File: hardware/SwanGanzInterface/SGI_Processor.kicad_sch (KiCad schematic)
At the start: 10 parts, among them U7 LP-MSPM0G3507, U8 Adafruit ST7735R

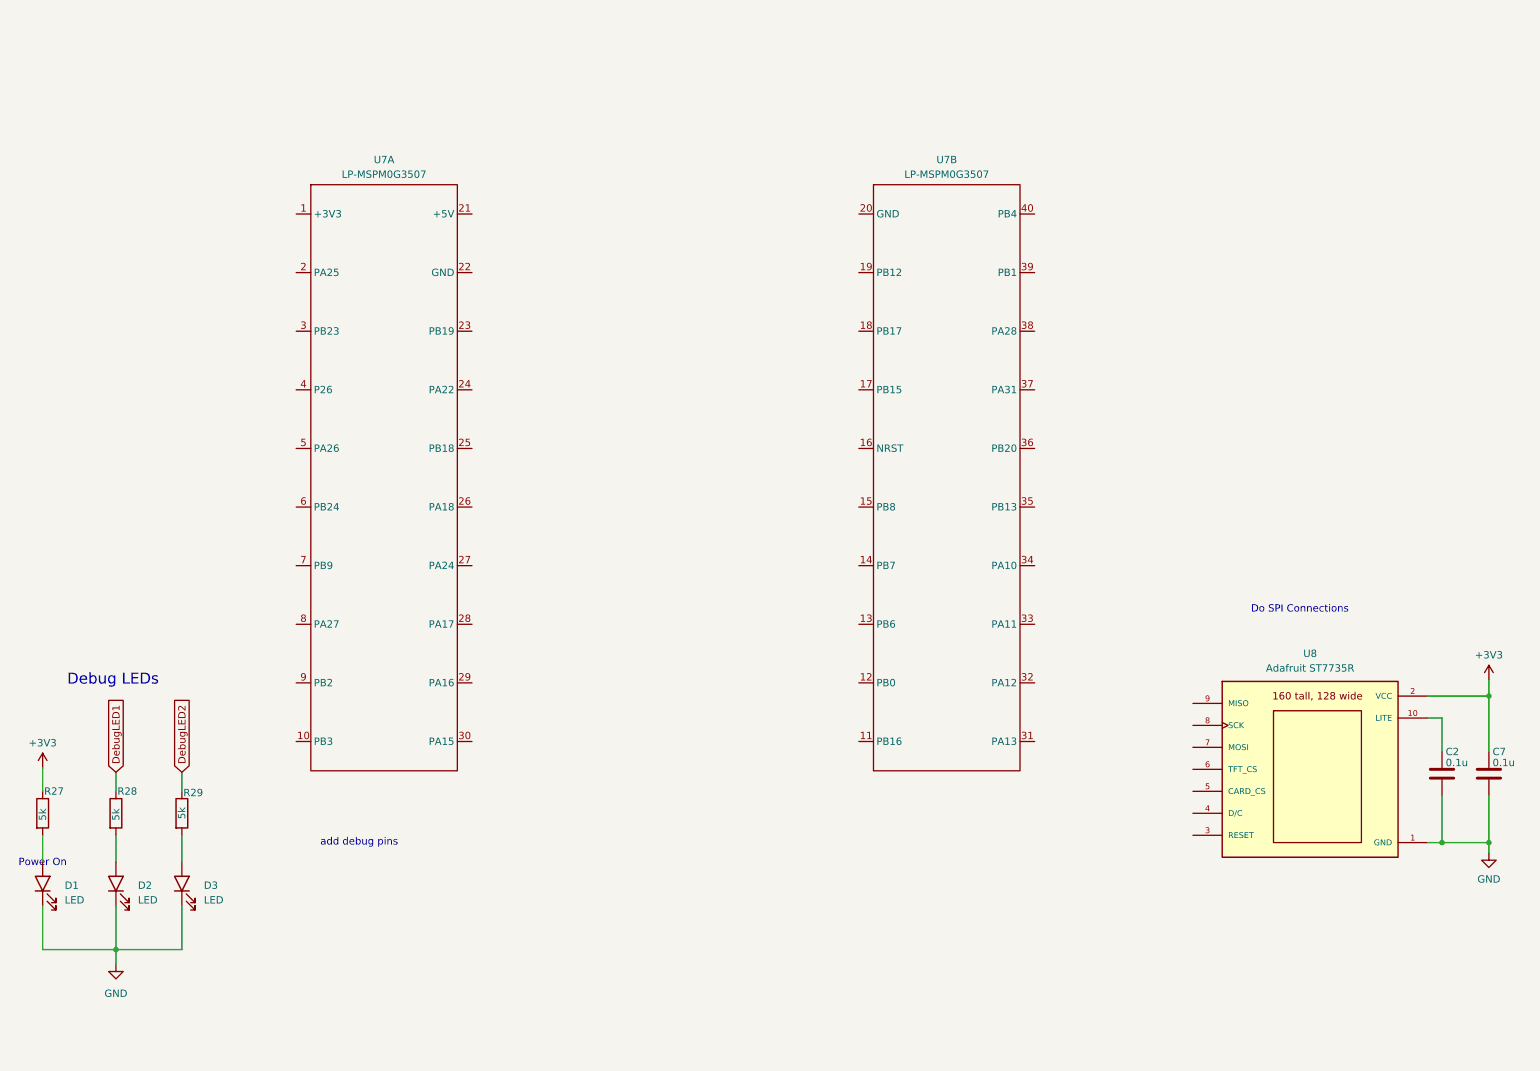
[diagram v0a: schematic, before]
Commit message: Added launchpad, power jumpers, messed with symbol lib
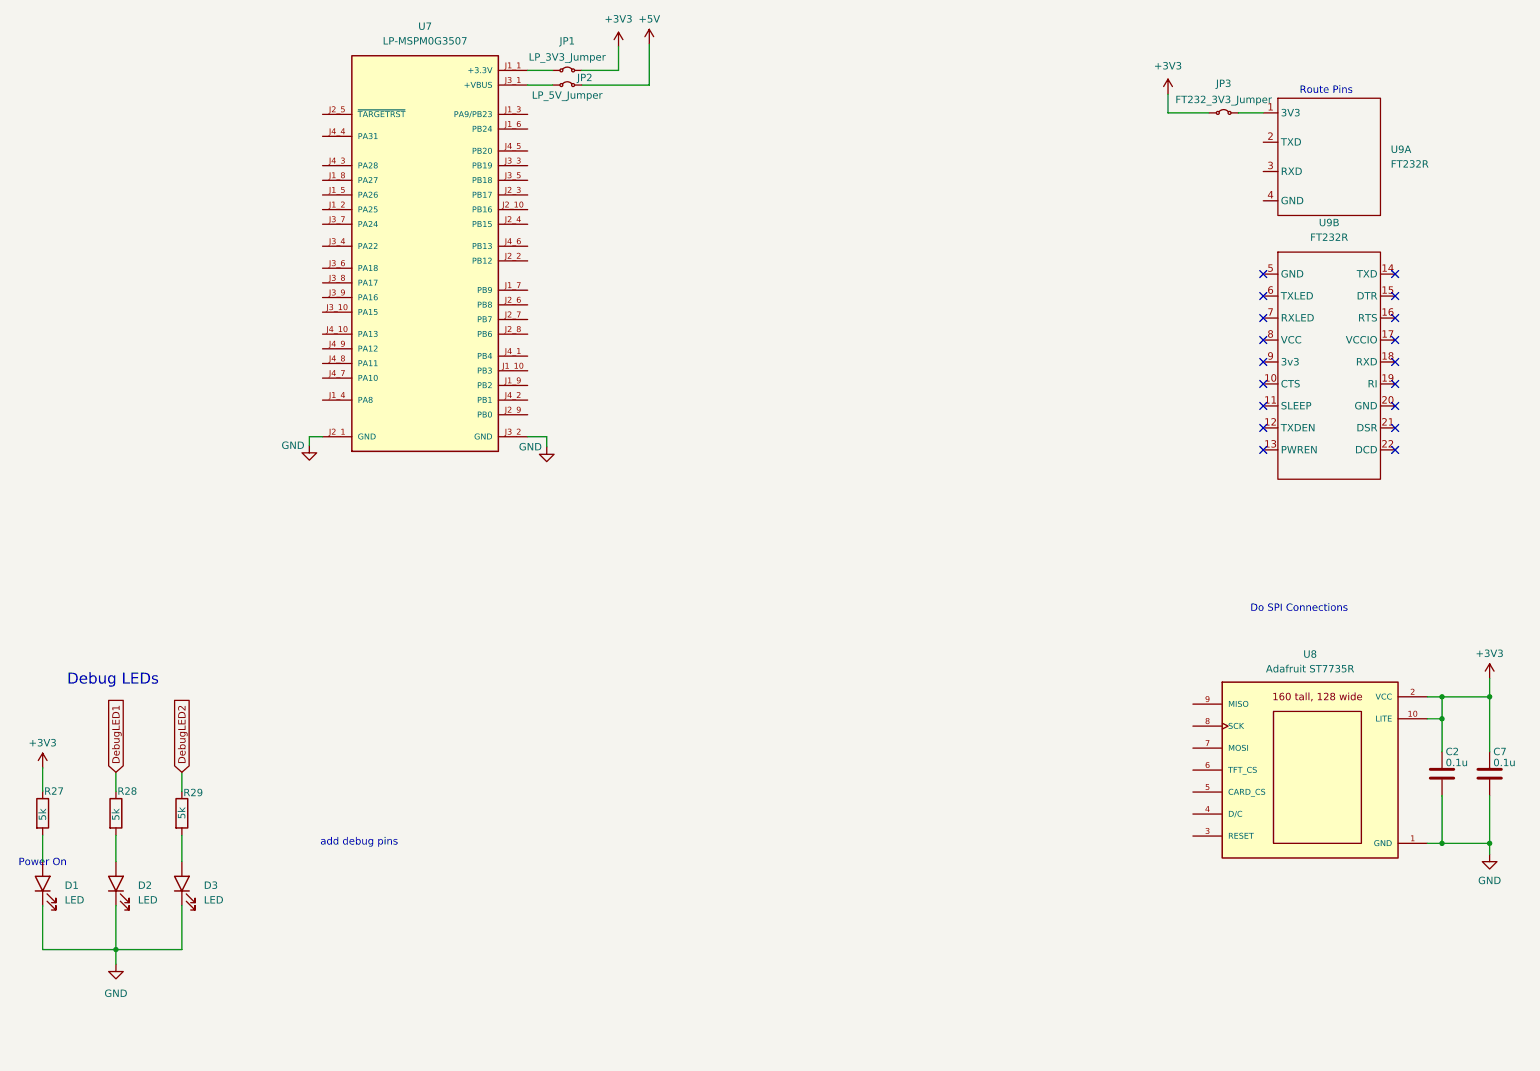
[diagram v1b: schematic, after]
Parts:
- removed unit 2 of U7
- added JP1: LP_3V3_Jumper, SGI_FootprintsLib:PinHeader_1x02_P2.54mm_Vertical, symbol Jumper:Jumper_2_Small_Bridged
- added JP2: LP_5V_Jumper, SGI_FootprintsLib:PinHeader_1x02_P2.54mm_Vertical, symbol Jumper:Jumper_2_Small_Bridged
- added JP3: FT232_3V3_Jumper, SGI_FootprintsLib:PinHeader_1x02_P2.54mm_Vertical, symbol Jumper:Jumper_2_Small_Bridged
- added U9: FT232R, SGI_FootprintsLib:FT232R-Breakout, symbol SGI_SymbolLib:FT232R-Breakout
- U7: footprint (none) -> SGI_FootprintsLib:ti_LP_MSPM0G3507; Cost (none) -> 22.60; Distributor (none) -> Mouser; Manufacturer (none) -> Texas Instruments; P/N (none) -> LP-MSPM0G3507
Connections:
- net +3V3: now also C2.1, U8.10 (LITE), JP1.2 (B), JP3.1 (A)
- net GND: now also U7.J2_1 (GND), U7.J3_2 (GND)
- new net: JP3.2 (B), U9.1 (3V3)
- new net: JP1.1 (A), U7.J1_1 (+3.3V)
- new net: JP2.1 (A), U7.J3_1 (+VBUS)
- new net +5V: JP2.2 (B)
- no-connect marks 0 -> 18
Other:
- note added: "Route Pins"

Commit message: Routed Microcontroller Schematic Pins
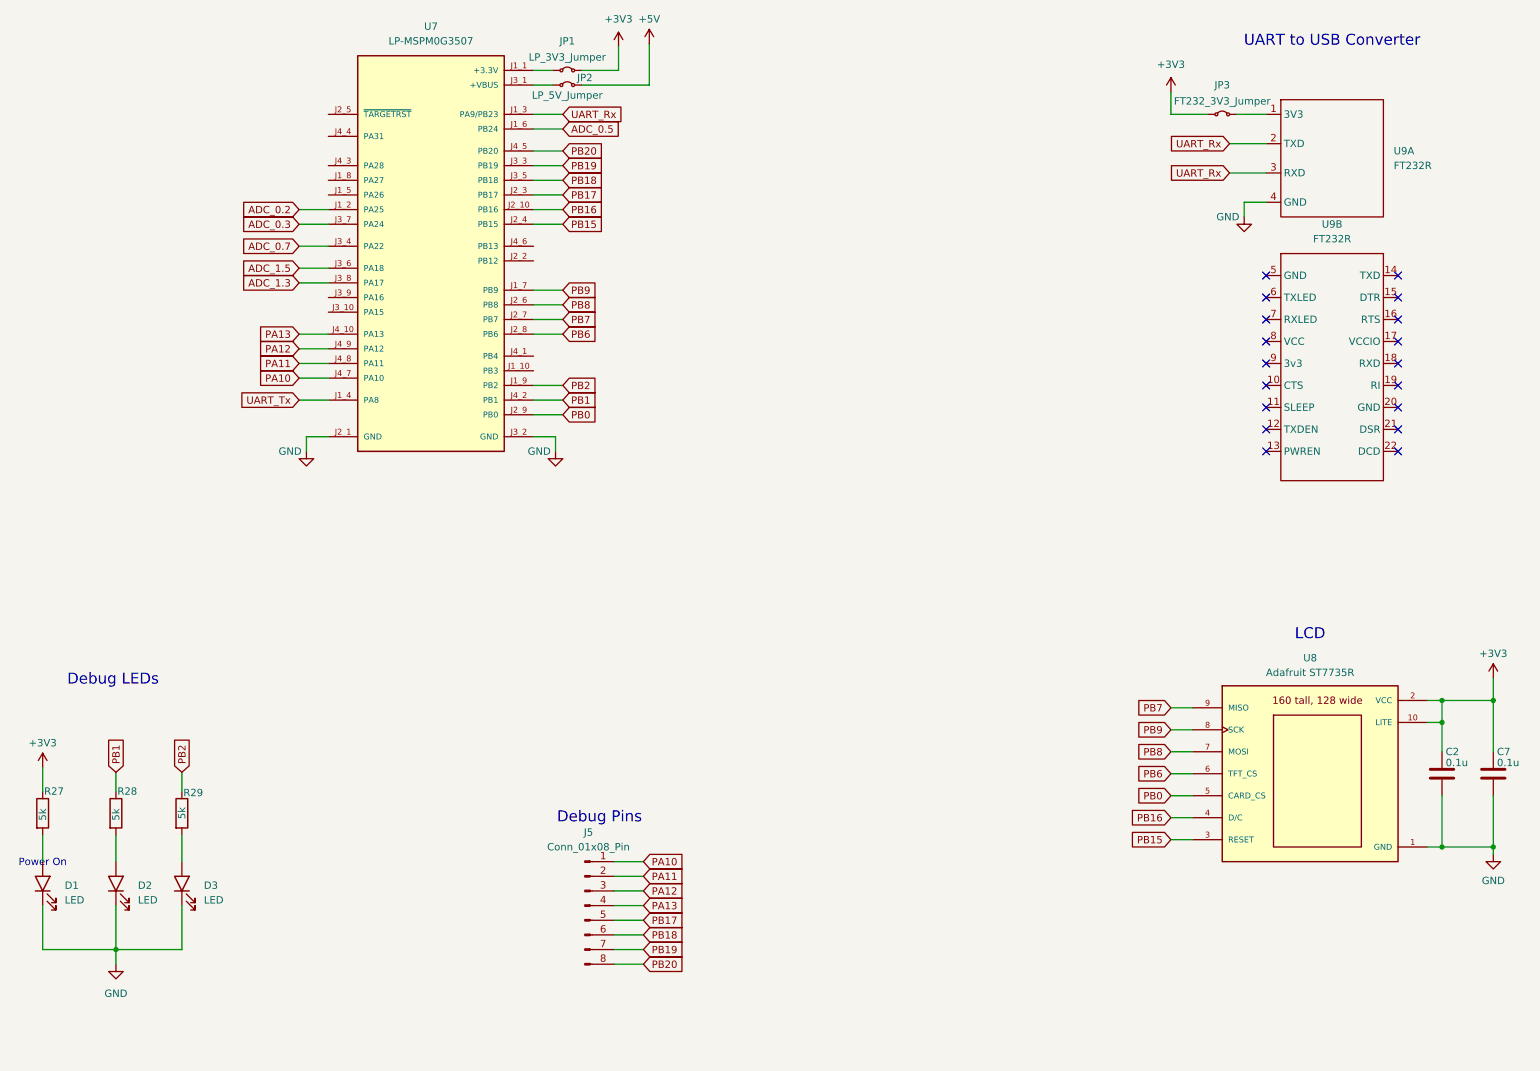
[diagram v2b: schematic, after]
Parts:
- added J5: Conn_01x08_Pin, symbol Connector:Conn_01x08_Pin
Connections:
- net DebugLED1 is gone; now on net PB1: R28.1
- net DebugLED2 is gone; now on net PB2: R29.1
- net GND: now also U9.4 (GND)
- net UART_Rx: now reaches U9.2 (TXD)
- net UART_Rx: now also U7.J1_3 (PA9/PB23), U9.3 (RXD)
- net PB15: now reaches U8.3 (RESET)
- net PB15: now also U7.J2_4 (PB15)
- net PB16: now reaches U8.4 (D/C)
- net PB16: now also U7.J2_10 (PB16)
- net PB0: now reaches U8.5 (CARD_CS)
- net PB0: now also U7.J2_9 (PB0)
- net PB6: now reaches U8.6 (TFT_CS)
- net PB6: now also U7.J2_8 (PB6)
- net PB8: now reaches U8.7 (MOSI)
- net PB8: now also U7.J2_6 (PB8)
- net PB9: now reaches U8.8 (SCK)
- net PB9: now also U7.J1_7 (PB9)
- net PB7: now reaches U8.9 (MISO)
- net PB7: now also U7.J2_7 (PB7)
- net ADC_0.2: now reaches U7.J1_2 (PA25)
- net UART_Tx: now reaches U7.J1_4 (PA8)
- net ADC_0.5: now reaches U7.J1_6 (PB24)
- net PB2: now reaches U7.J1_9 (PB2)
- net PB17: now reaches U7.J2_3 (PB17)
- net PB17: now also J5.5 (Pin_5)
- net PB19: now reaches U7.J3_3 (PB19)
- net PB19: now also J5.7 (Pin_7)
- net ADC_0.7: now reaches U7.J3_4 (PA22)
- net PB18: now reaches U7.J3_5 (PB18)
- net PB18: now also J5.6 (Pin_6)
- net ADC_1.5: now reaches U7.J3_6 (PA18)
- net ADC_0.3: now reaches U7.J3_7 (PA24)
- net ADC_1.3: now reaches U7.J3_8 (PA17)
- net PA13: now reaches U7.J4_10 (PA13)
- net PA13: now also J5.4 (Pin_4)
- net PB1: now reaches U7.J4_2 (PB1)
- net PB20: now reaches U7.J4_5 (PB20)
- net PB20: now also J5.8 (Pin_8)
- net PA10: now reaches U7.J4_7 (PA10)
- net PA10: now also J5.1 (Pin_1)
- net PA11: now reaches U7.J4_8 (PA11)
- net PA11: now also J5.2 (Pin_2)
- net PA12: now reaches U7.J4_9 (PA12)
- net PA12: now also J5.3 (Pin_3)
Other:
- note added: "Debug Pins"
- note added: "LCD"
- note added: "UART to USB Converter"
- note removed: "Do SPI Connections"
- note removed: "Route Pins"
- note removed: "add debug pins"
- moved on the sheet: C7, U7, U8, U9A, U9B
